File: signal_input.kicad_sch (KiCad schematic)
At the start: 32 parts, among them IC1 TXU0104QWBQARQ1, IC2 TXU0104QWBQARQ1, IC3 TXU0104QWBQARQ1, IC4 TXU0104QWBQARQ1, J4 6101XX249121_610108249121, J5 6101XX249121_610108249121, J6 6101XX249121_610108249121, J7 6101XX249121_610108249121

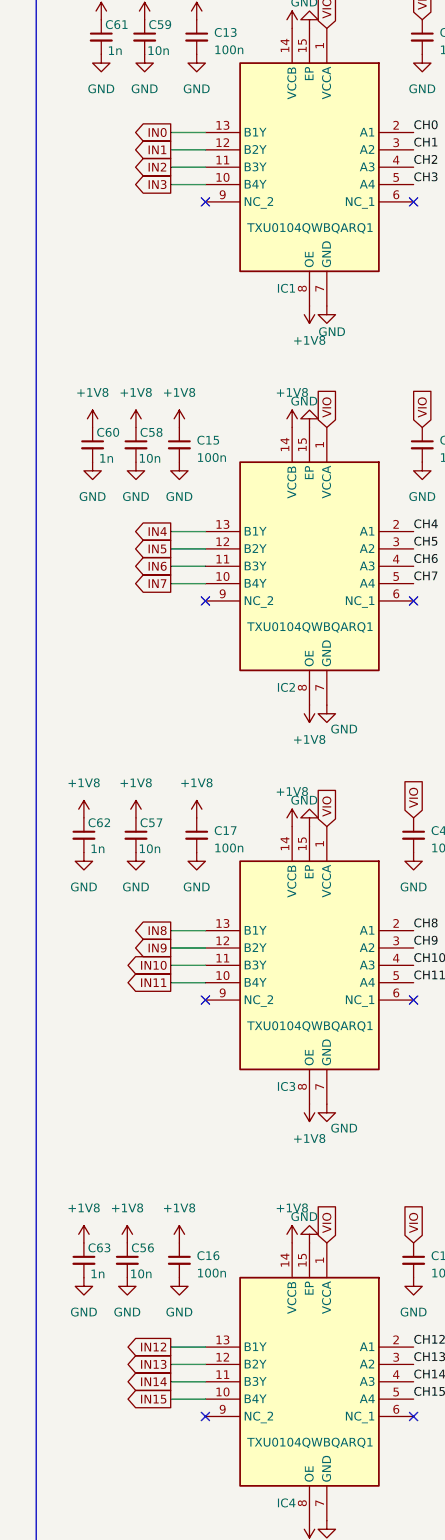
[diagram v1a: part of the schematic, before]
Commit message: start reworking the usb3c to add ESD and better impedance matching
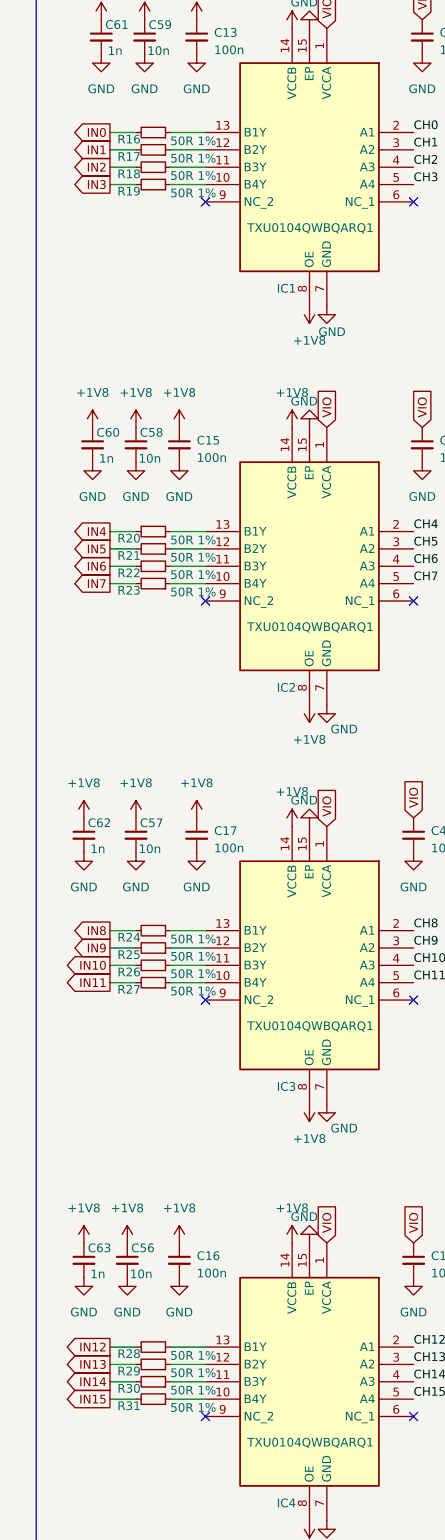
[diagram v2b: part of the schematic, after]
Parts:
- added R16, R17, R18, R19, R20, R21, R22, R23, R24, R25, R26, R27, R28, R29, R30, R31: 50R 1%, Resistor_SMD:R_0201_0603Metric, symbol Device:R_Small
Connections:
- net IN0: now also R16.2; no longer IC1.13 (B1Y)
- net IN1: now also R17.2; no longer IC1.12 (B2Y)
- net IN10: now also R26.2; no longer IC3.11 (B3Y)
- net IN11: now also R27.2; no longer IC3.10 (B4Y)
- net IN12: now also R28.2; no longer IC4.13 (B1Y)
- net IN13: now also R29.2; no longer IC4.12 (B2Y)
- net IN14: now also R30.2; no longer IC4.11 (B3Y)
- net IN15: now also R31.2; no longer IC4.10 (B4Y)
- net IN2: now also R18.2; no longer IC1.11 (B3Y)
- net IN3: now also R19.2; no longer IC1.10 (B4Y)
- net IN4: now also R20.2; no longer IC2.13 (B1Y)
- net IN5: now also R21.2; no longer IC2.12 (B2Y)
- net IN6: now also R22.2; no longer IC2.11 (B3Y)
- net IN7: now also R23.2; no longer IC2.10 (B4Y)
- net IN8: now also R24.2; no longer IC3.13 (B1Y)
- net IN9: now also R25.2; no longer IC3.12 (B2Y)
- new net: IC1.10 (B4Y), R19.1
- new net: IC1.11 (B3Y), R18.1
- new net: IC1.12 (B2Y), R17.1
- new net: IC1.13 (B1Y), R16.1
- new net: IC2.11 (B3Y), R22.1
- new net: IC4.13 (B1Y), R28.1
- new net: IC4.10 (B4Y), R31.1
- new net: IC4.11 (B3Y), R30.1
- new net: IC4.12 (B2Y), R29.1
- new net: IC3.12 (B2Y), R25.1
- new net: IC3.10 (B4Y), R27.1
- new net: IC3.11 (B3Y), R26.1
- new net: IC3.13 (B1Y), R24.1
- new net: IC2.12 (B2Y), R21.1
- new net: IC2.13 (B1Y), R20.1
- new net: IC2.10 (B4Y), R23.1
